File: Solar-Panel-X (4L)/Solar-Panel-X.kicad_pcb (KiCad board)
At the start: 4 copper layers, 48.4 x 48.4 mm, 81 parts, among them J1 FTS-105-01-L-DV-A, Q1 BSS138DWQ-7, Q2 MBT2222ADW1T1, Q3 BSS138DWQ-7, Q4 MBT2222ADW1T1, U1 BQ25570RGRR, U2 TSL2561

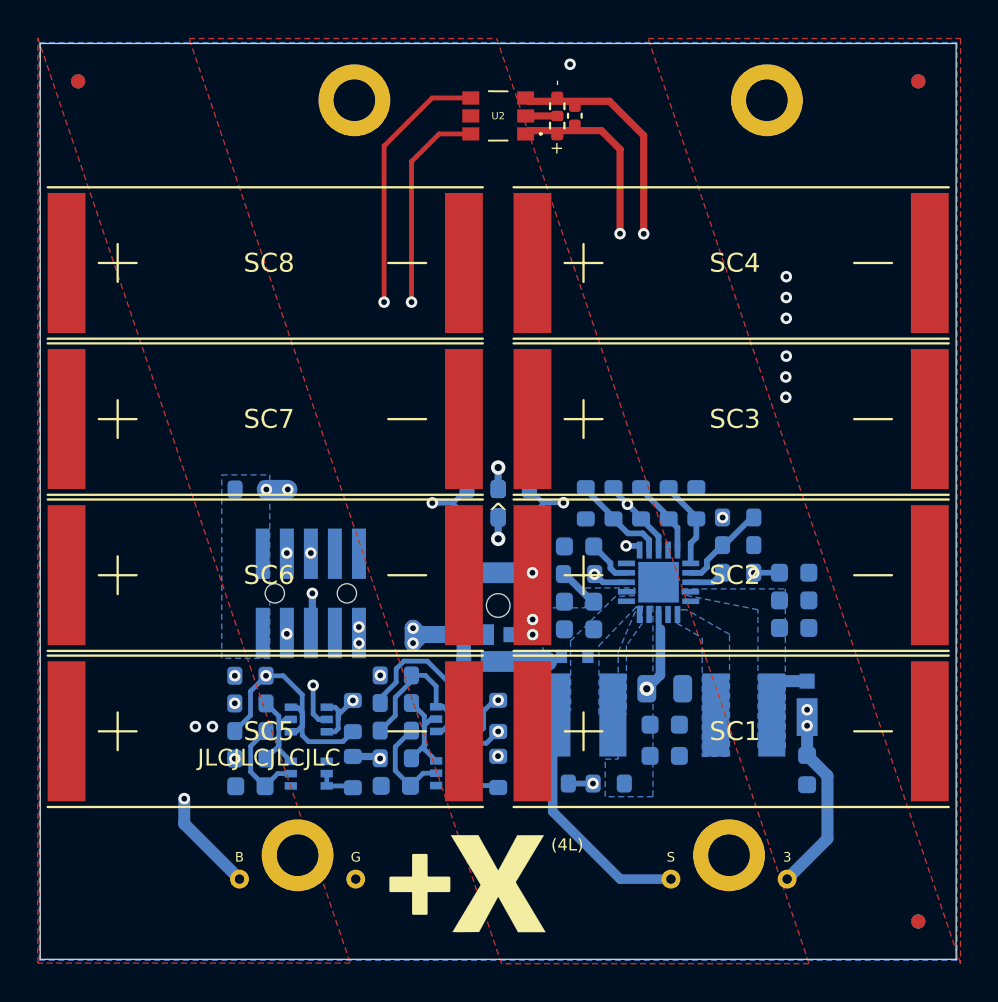
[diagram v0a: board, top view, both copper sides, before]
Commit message: Changed TSL2591 to BH1750
All boards (4L) except -Y
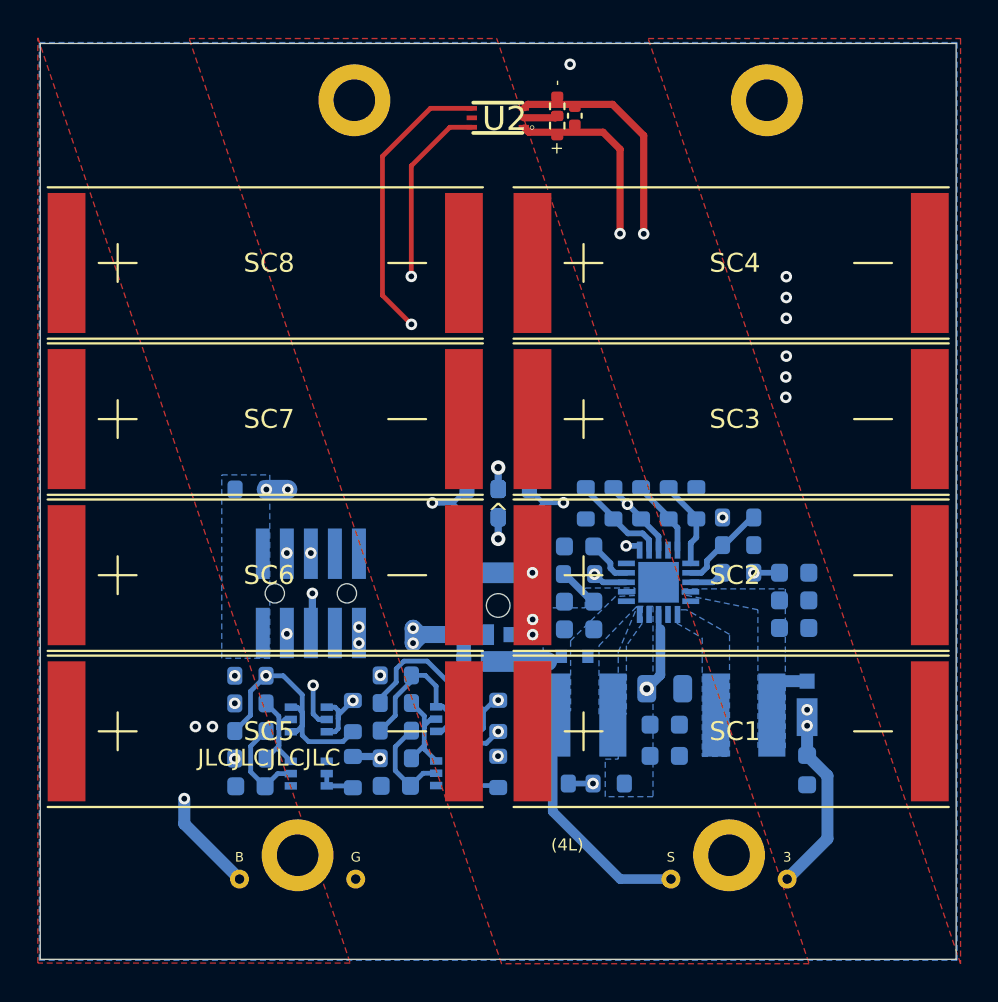
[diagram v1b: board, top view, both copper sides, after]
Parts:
- removed REF** (x6): Fiducial_0.75mm_Mask1.5mm, Fiducial:Fiducial_0.75mm_Mask1.5mm
- removed REF**: X Label, X Label
- removed Ref**: Val**, custom-footprints:pycubed_mini_half
- U2: value TSL2561 -> BH1750FVI-TR; footprint solarpanels:TSL2561 -> solarpanels:WSOF6
- moved U2 0.10 mm to (106.7, 46.2)
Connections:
- R5 pad 1: Net-(R5-Pad1) -> Net-(R10-Pad2)
- R6 pad 2: Net-(R5-Pad1) -> Net-(R10-Pad2)
- U1 pad 7: Net-(R5-Pad1) -> Net-(R10-Pad2)
- U2 pad 4: SCL_LS -> SDA_LS
- U2 pad 6: SDA_LS -> SCL_LS
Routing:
- net Net-(R10-Pad2): track 9.42 -> 14.4 mm
- net Net-(R5-Pad1): track 4.95 -> 0.00 mm
- net SDA_LS: track 47.5 -> 50.5 mm
- net SCL_LS: track 50.3 -> 48.2 mm

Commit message: Updated light sensor to OPT 3001, Updated solar diodes.
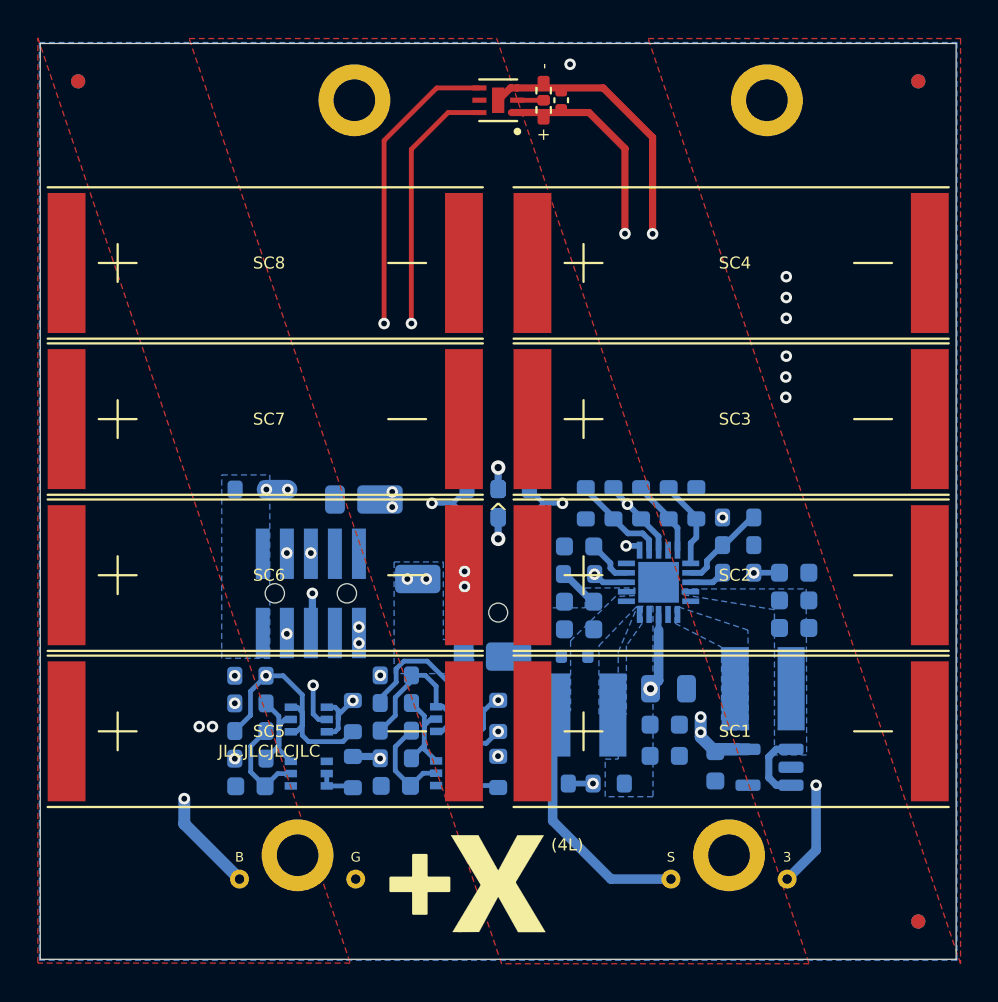
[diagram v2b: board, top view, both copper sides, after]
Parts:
- removed D5: MSS1P4-M3_89A, solarpanels:MICROSMP
- added REF**: Fiducial_0.75mm_Mask1.5mm, Fiducial:Fiducial_0.75mm_Mask1.5mm, F.Cu at (128.9, 88.7)
- added REF**: Fiducial_0.75mm_Mask1.5mm, Fiducial:Fiducial_0.75mm_Mask1.5mm, F.Cu at (128.9, 44.3)
- added REF**: Fiducial_0.75mm_Mask1.5mm, Fiducial:Fiducial_0.75mm_Mask1.5mm, F.Cu at (84.5, 44.3)
- added REF**: X Label, X Label, F.Cu at (106.7, 88.2)
- added REF**: Fiducial_0.75mm_Mask1.5mm, Fiducial:Fiducial_0.75mm_Mask1.5mm, B.Cu at (84.5, 44.3)
- added REF**: Fiducial_0.75mm_Mask1.5mm, Fiducial:Fiducial_0.75mm_Mask1.5mm, B.Cu at (128.9, 88.7)
- added REF**: Fiducial_0.75mm_Mask1.5mm, Fiducial:Fiducial_0.75mm_Mask1.5mm, B.Cu at (128.9, 44.3)
- added Ref**: Val**, custom-footprints:pycubed_mini_half, B.Cu at (107.0, 44.5)
- added U3: MAX40200AUK, Package_TO_SOT_SMD:SOT-23-5, B.Cu at (121.0, 80.5)
- C1: value 1uF -> 0.1uF
- D2, D3, D4: value MSS1P4-M3_89A -> DFLS130L-7; footprint solarpanels:MICROSMP -> Diode_SMD:D_PowerDI-123
- J1: value FTS-105-01-L-DV-A -> FTS-105-01-X-DV-A
- Q1, Q3: value BSS138DWQ-7 -> NX3008NBKS
- R1, R12, R13, R16, R17, R18, R2, R3, R4: value 0 -> 0R
- R14, R15, R19, R20: value DNI -> DNI (0R)
- R21, R26: value 680 -> 680R
- U2: value BH1750FVI-TR -> OPT3001; footprint solarpanels:WSOF6 -> solarpanels:OPT3001
- moved D2 16.8 mm to (106.4, 74.7), turned to 180 degrees
- moved D3 7.59 mm to (99.6, 66.4)
- moved C11 4.85 mm to (118.2, 80.5)
- moved D4 4.08 mm to (103.3, 70.6)
- moved L2 1.72 mm to (120.7, 76.4)
- moved R1 1.10 mm to (109.1, 45.8)
- moved R2 1.10 mm to (109.1, 44.8)
- moved C1 1.09 mm to (110.0, 45.3)
- moved U2 0.93 mm to (106.7, 45.3)
- moved C5 0.20 mm to (115.7, 76.4)
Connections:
- C10 pad 1: Net-(C10-Pad1) -> Net-(U1-VOUT)
- C8 pad 1: Net-(C10-Pad1) -> Net-(U1-VOUT)
- D2 pad 1: +3V3 -> VSOLAR
- D2 pad 2: Net-(C10-Pad1) -> /VSOLAR_FULL
- L2 pad 2: Net-(C10-Pad1) -> Net-(U1-VOUT)
- R10 pad 2: Net-(R10-Pad2) -> Net-(U1-VRDIV)
- R5 pad 1: Net-(R10-Pad2) -> Net-(U1-VBAT_OV)
- R5 pad 2: Net-(R10-Pad2) -> Net-(U1-VRDIV)
- R6 pad 2: Net-(R10-Pad2) -> Net-(U1-VBAT_OV)
- R7 pad 2: Net-(R10-Pad2) -> Net-(U1-VRDIV)
- U1 pad 14: Net-(C10-Pad1) -> Net-(U1-VOUT)
- U1 pad 7: Net-(R10-Pad2) -> Net-(U1-VBAT_OV)
- U1 pad 8: Net-(R10-Pad2) -> Net-(U1-VRDIV)
- U2 pad 4: SDA_LS -> SCL_LS
- U2 pad 6: SCL_LS -> SDA_LS
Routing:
- net Net-(R10-Pad2): track 14.4 -> 0.00 mm, vias 2 -> 0
- net Net-(U1-VRDIV): track 0.00 -> 9.42 mm, vias 0 -> 2
- net Net-(U1-VBAT_OV): track 0.00 -> 4.95 mm
- net /VSOLAR_FULL: track 24.3 -> 20.5 mm
- net Net-(U1-VOUT): track 0.00 -> 3.78 mm
- net Net-(D3-K): track 3.67 -> 0.00 mm, vias 3 -> 4
- net +3V3: track 20.7 -> 23.2 mm, vias 10 -> 11
- net GND: track 12.3 -> 14.6 mm
- net VSOLAR: track 17.2 -> 15.0 mm
- net SCL_LS: track 48.2 -> 50.3 mm
- net Net-(C10-Pad1): track 1.87 -> 0.00 mm
- net SDA_LS: track 50.5 -> 48.9 mm
- net /coil: track 6615.5 -> 6614.4 mm
- net VBAT: track 11.1 -> 10.5 mm
- added copper zone on B.Cu, net /VSOLAR_FULL
- added copper zone on B.Cu, net Net-(U1-VOUT)
- removed copper zone on B.Cu, net Net-(C10-Pad1)
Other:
- outline, holes or cut-outs redrawn
- board text added: "Rev B3/01"
- board text removed: "Rev B2/01"

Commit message: Updated Mounting Holes
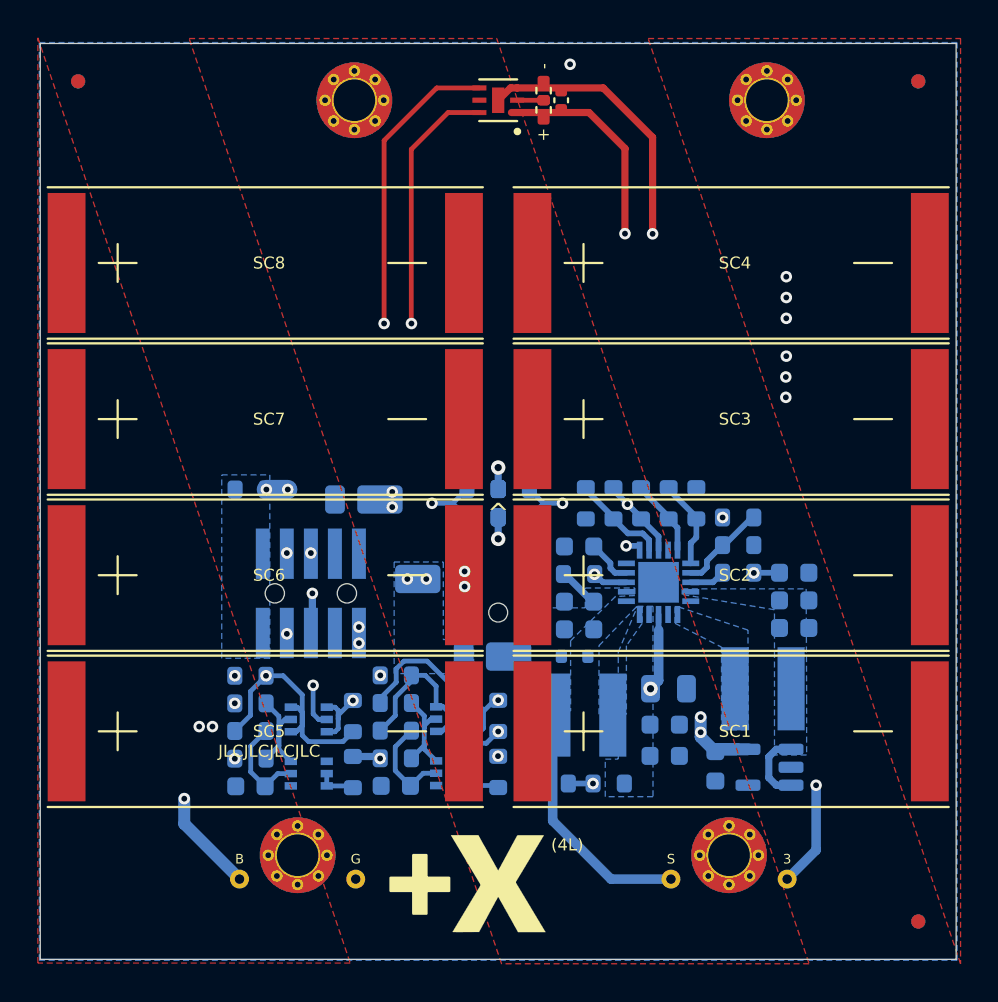
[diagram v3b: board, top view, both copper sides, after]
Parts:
- H1, H2, H3, H4: footprint MountingHole:MountingHole_2.2mm_M2_DIN965_Pad -> solarpanels:MountingHole_2.2mm_M2_DIN965_Pad_TopBottom; moved to F.Cu
- turned H1 to 0 degrees
- turned H2 to 0 degrees
- turned H3 to 0 degrees
- turned H4 to 0 degrees

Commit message: B3/02 Updates
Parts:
- REF** (x6): value Fiducial_0.75mm_Mask1.5mm -> Fiducial_1mm_Mask2mm; footprint Fiducial:Fiducial_0.75mm_Mask1.5mm -> Fiducial:Fiducial_1mm_Mask2mm
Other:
- outline, holes or cut-outs redrawn
- board text added: "Rev B3/02"
- board text removed: "Rev B3/01"

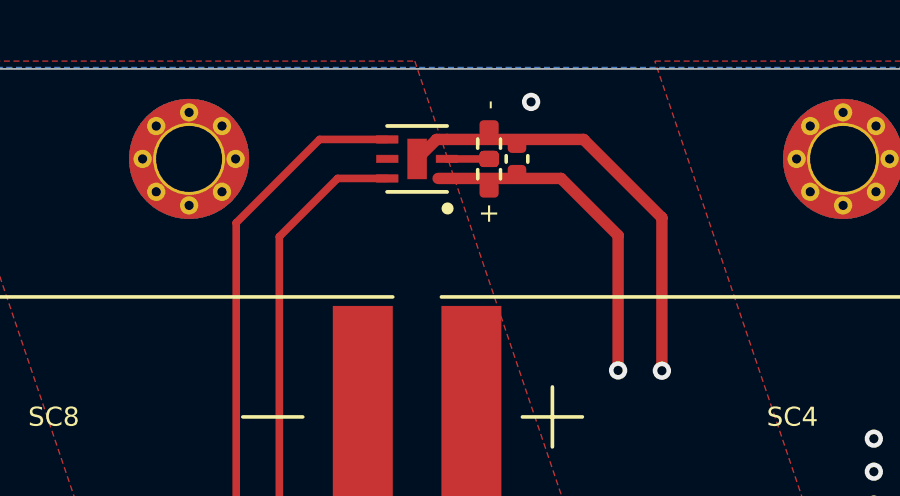
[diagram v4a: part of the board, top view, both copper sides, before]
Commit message: Updated Sun Sensor to OPT4001
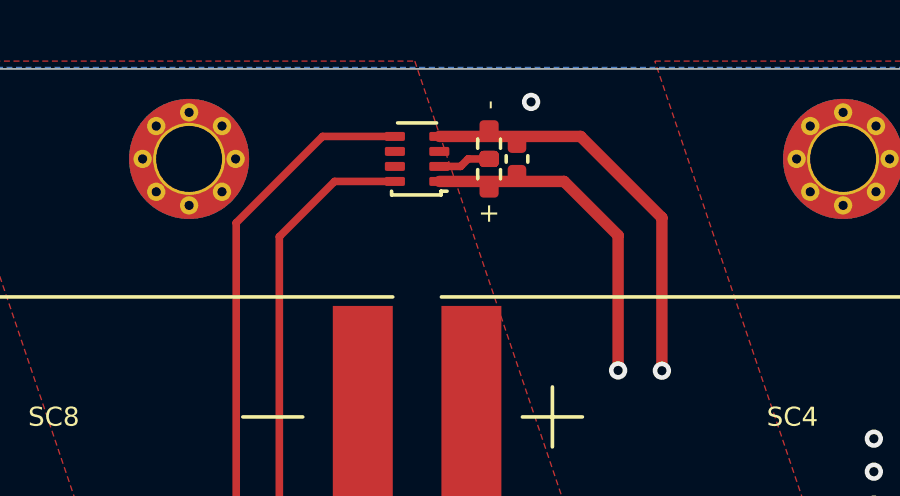
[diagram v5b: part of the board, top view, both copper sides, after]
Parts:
- U2: value OPT3001 -> OPT4001; footprint solarpanels:OPT3001 -> Package_TO_SOT_SMD:SOT-583-8
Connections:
- U2 pad 3: GND -> unconnected-(U2-NC-Pad3)
- U2 pad 4: SCL_LS -> GND
- U2 pad 5: unconnected-(U2-INT-Pad5) -> SCL_LS
- U2 pad 6: SDA_LS -> unconnected-(U2-NC-Pad6)
- U2 pad 7: GND -> unconnected-(U2-INT-Pad7)
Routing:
- net GND: track 14.6 -> 13.6 mm

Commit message: Updated Rev to B3/03
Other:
- board text added: "Rev B3/03"
- board text removed: "Rev B3/02"
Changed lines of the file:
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@@
     (effects (font (size 0.635 0.635) (thickness 0.1016)))
   )
-  (gr_text "Rev B3/02" (at 106.7 46.625) (layer "B.Mask")
+  (gr_text "Rev B3/03" (at 106.7 46.625) (layer "B.Mask")
     (effects (font (size 0.635 0.635) (thickness 0.1524)) (justify mirror))
   )

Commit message: Exported stuff
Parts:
- added ?: , clipboard:eb50a26b-5fb6-463a-8dd0-ee5887daaa13, F.Cu at (102.6, 85.2)
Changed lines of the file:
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@@
       (drillshape 0)
       (scaleselection 1)
-      (outputdirectory "../../Gerbers/-X")
+      (outputdirectory "../../Gerbers/+X")
     )
   )
@@
       (net 1 "GND") (pinfunction "1") (pintype "input"))
   )
+  (footprint "clipboard:eb50a26b-5fb6-463a-8dd0-ee5887daaa13" (layer "F.Cu")
+    (at 102.56 85.19)
+    (fp_text reference "" (at 0 0) (layer "F.SilkS")
+        (effects (font (size 1.27 1.27) (thickness 0.15)))
+    )
+    (fp_text value "" (at 0 0) (layer "F.SilkS")
+        (effects (font (size 1.27 1.27) (thickness 0.15)))
+    )
+    (fp_rect (start -0.35 0) (end 0.35 3.1)
+      (stroke (width 0.12) (type solid)) (fill solid) (layer "F.SilkS"))
+  )
   (footprint "solarpanels:KXOB25-05X3F" (layer "F.Cu")
     (at 83.89 53.9)
@@
         (effects (font (size 1 1) (thickness 0.15)))
     )
-    (fp_rect (start -4.4902 -3.0176) (end -3.7902 0.0824)
-      (stroke (width 0.12) (type solid)) (fill solid) (layer "F.SilkS"))
     (fp_rect (start -2.5902 -1.1176) (end -5.6902 -1.8176)
       (stroke (width 0.12) (type solid)) (fill solid) (layer "F.SilkS"))
@@
     (pts (xy 82.5 42.3) (xy 82.5 90.7))
     (height 3.499999)
-    (gr_text "1905.5118 mils" (at 77.850001 66.5 90) (layer "Dwgs.User")
+    (gr_text "48.4000 mm" (at 77.850001 66.5 90) (layer "Dwgs.User")
       (effects (font (size 1 1) (thickness 0.15)))
     )
@@
     (pts (xy 82.5 42.3) (xy 130.9 42.3))
     (height -3.6)
-    (gr_text "1905.5118 mils" (at 106.7 37.55) (layer "Dwgs.User")
+    (gr_text "48.4000 mm" (at 106.7 37.55) (layer "Dwgs.User")
       (effects (font (size 1 1) (thickness 0.15)))
     )
